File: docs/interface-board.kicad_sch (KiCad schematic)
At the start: 12 parts, among them J1 ESC-L-XBUS, J2 ESC-R-XBUS, J3 XBUS-TX-OUT, J4 XBUS-RX-OUT, J5 RECEIVER-SBUS, J6 SBUS-OUT, Q1 2N3904

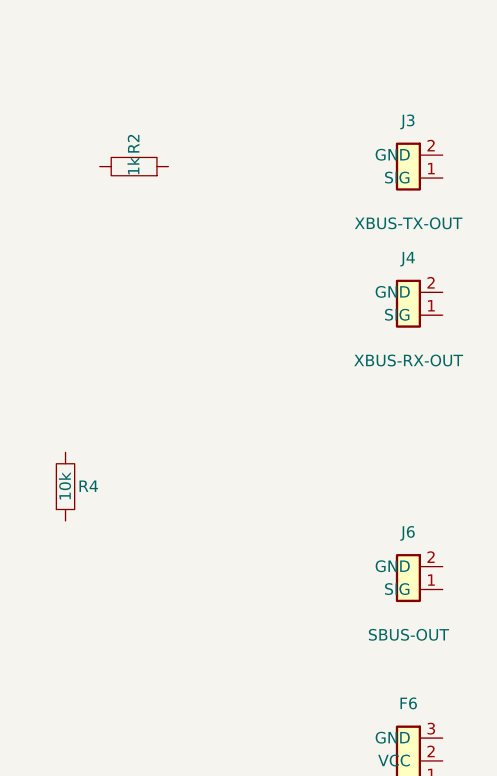
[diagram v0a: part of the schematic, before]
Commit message: review: fix markdownlint, F6 labeling, A4/A5 note, KiCad 3-pin, defaults clarity
- Fix markdown table spacing and blank-line-before-list (markdownlint MD060/MD032)
- Fix "timeout" → "time out" verb form
- F6 power connector: label pin numbers explicitly to avoid confusion
  with standard Signal/VCC/GND column headers
- A4/A5: relabel from "Free" to "I2C SDA/SCL" (they are dedicated I2C)
- GL10 defaults: clarify table shows factory defaults, not our tuned values
- KiCad schematic: J3/J4/J6 changed from Conn_01x02 to Conn_01x03
  to match the all-3-pin-servo standardization

Co-Authored-By: Claude Opus 4.7 (1M context) <noreply@anthropic.com>
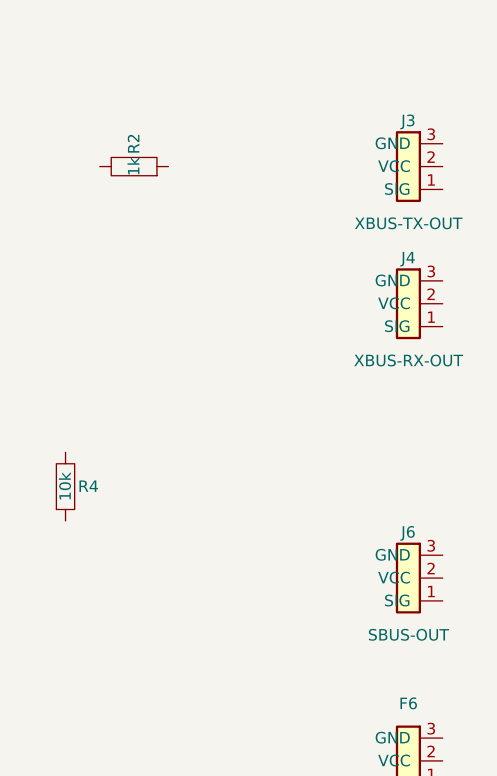
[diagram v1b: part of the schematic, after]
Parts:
- J3, J4, J6: symbol Conn_01x02 -> Conn_01x03
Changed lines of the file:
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@@
     (property "Reference" "J5" (at 25.4 92.71 0))
     (property "Value" "RECEIVER-SBUS" (at 25.4 80.01 0)))
-  (symbol (lib_id "Conn_01x02") (at 139.7 40.64 180) (unit 1)
+  (symbol (lib_id "Conn_01x03") (at 139.7 40.64 180) (unit 1)
     (property "Reference" "J3" (at 139.7 35.56 0))
     (property "Value" "XBUS-TX-OUT" (at 139.7 46.99 0)))
-  (symbol (lib_id "Conn_01x02") (at 139.7 55.88 180) (unit 1)
+  (symbol (lib_id "Conn_01x03") (at 139.7 55.88 180) (unit 1)
     (property "Reference" "J4" (at 139.7 50.8 0))
     (property "Value" "XBUS-RX-OUT" (at 139.7 62.23 0)))
-  (symbol (lib_id "Conn_01x02") (at 139.7 86.36 180) (unit 1)
+  (symbol (lib_id "Conn_01x03") (at 139.7 86.36 180) (unit 1)
     (property "Reference" "J6" (at 139.7 81.28 0))
     (property "Value" "SBUS-OUT" (at 139.7 92.71 0)))
